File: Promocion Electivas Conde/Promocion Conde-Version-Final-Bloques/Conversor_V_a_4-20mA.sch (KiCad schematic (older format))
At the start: 11 parts

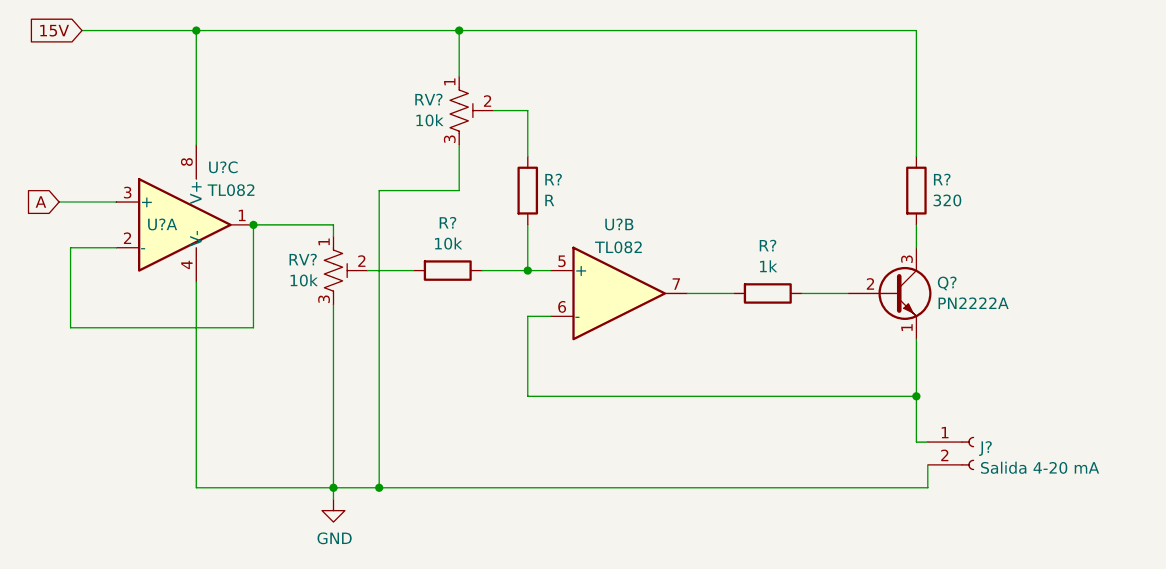
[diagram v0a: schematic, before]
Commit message: Bloques y footprint asignados
Falta elegir y asignar el de los potenciometros Rv3 y Rv7.
Las salidas K3 y K20 también...
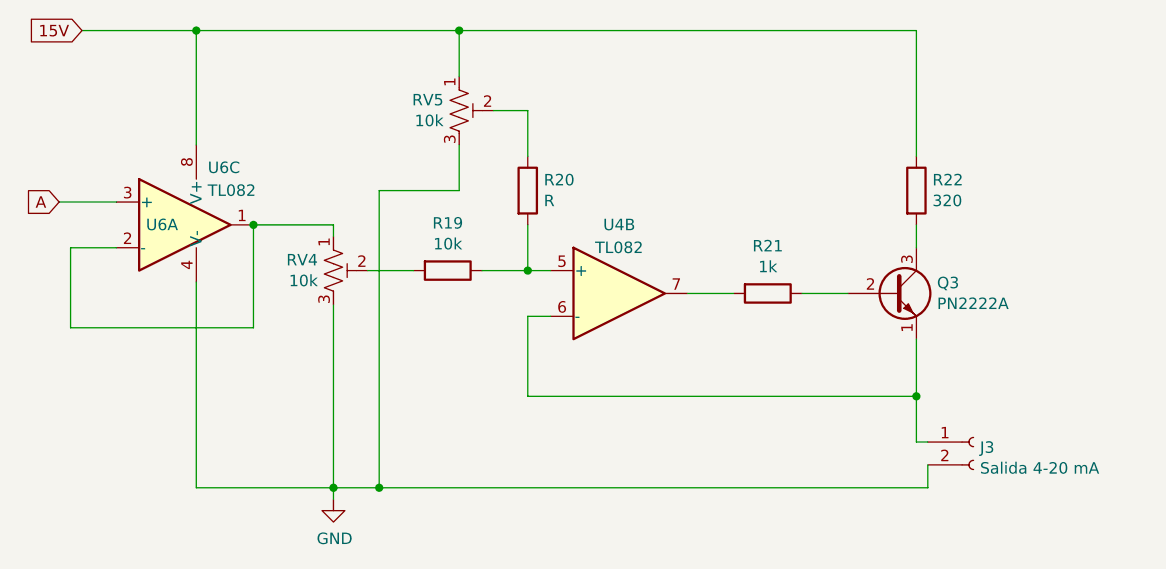
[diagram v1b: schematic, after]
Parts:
- R19, R20, R21, R22: renamed from R?; footprint (none) -> Resistor_SMD:R_0603_1608Metric_Pad0.98x0.95mm_HandSolder
- RV4, RV5: renamed from RV?; footprint (none) -> Resistor_SMD:R_0603_1608Metric_Pad0.98x0.95mm_HandSolder
- U4, U6: renamed from U?; footprint (none) -> Package_SO:SOIC-8-1EP_3.9x4.9mm_P1.27mm_EP2.29x3mm
- gave numbers to parts that had none: 2
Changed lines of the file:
@@
 $Descr A4 11693 8268
 encoding utf-8
-Sheet 5 5
+Sheet 3 6
 Title ""
 Date ""
@@
 $EndDescr
 $Comp
-L Device:R_POT_TRIM_US RV?
+L Device:R_POT_TRIM_US RV4
 U 1 1 61856B19
 P 3250 3750
-F 0 "RV?" H 3182 3796 50  0000 R CNN
+F 0 "RV4" H 3182 3796 50  0000 R CNN
 F 1 "10k" H 3182 3705 50  0000 R CNN
-F 2 "" H 3250 3750 50  0001 C CNN
+F 2 "Resistor_SMD:R_0603_1608Metric_Pad0.98x0.95mm_HandSolder" H 3250 3750 50  0001 C CNN
 F 3 "~" H 3250 3750 50  0001 C CNN
 	1    3250 3750
@@
 $EndComp
 $Comp
-L Device:R_POT_TRIM_US RV?
+L Device:R_POT_TRIM_US RV5
 U 1 1 6185887C
 P 3800 3050
-F 0 "RV?" H 3732 3096 50  0000 R CNN
+F 0 "RV5" H 3732 3096 50  0000 R CNN
 F 1 "10k" H 3732 3005 50  0000 R CNN
-F 2 "" H 3800 3050 50  0001 C CNN
+F 2 "Resistor_SMD:R_0603_1608Metric_Pad0.98x0.95mm_HandSolder" H 3800 3050 50  0001 C CNN
 F 3 "~" H 3800 3050 50  0001 C CNN
 	1    3800 3050
@@
 $EndComp
 $Comp
-L Device:R R?
+L Device:R R21
 U 1 1 61859CCC
 P 5150 3850
-F 0 "R?" V 4943 3850 50  0000 C CNN
+F 0 "R21" V 4943 3850 50  0000 C CNN
 F 1 "1k" V 5034 3850 50  0000 C CNN
-F 2 "" V 5080 3850 50  0001 C CNN
+F 2 "Resistor_SMD:R_0603_1608Metric_Pad0.98x0.95mm_HandSolder" V 5080 3850 50  0001 C CNN
 F 3 "~" H 5150 3850 50  0001 C CNN
 	1    5150 3850
@@
 $EndComp
 $Comp
-L Device:R R?
+L Device:R R22
 U 1 1 61859D46
 P 5800 3400
-F 0 "R?" H 5870 3446 50  0000 L CNN
+F 0 "R22" H 5870 3446 50  0000 L CNN
 F 1 "320" H 5870 3355 50  0000 L CNN
-F 2 "" V 5730 3400 50  0001 C CNN
+F 2 "Resistor_SMD:R_0603_1608Metric_Pad0.98x0.95mm_HandSolder" V 5730 3400 50  0001 C CNN
 F 3 "~" H 5800 3400 50  0001 C CNN
 	1    5800 3400
@@
 $EndComp
 $Comp
-L Device:R R?
+L Device:R R20
 U 1 1 6185A023
 P 4100 3400
-F 0 "R?" H 4170 3446 50  0000 L CNN
+F 0 "R20" H 4170 3446 50  0000 L CNN
 F 1 "R" H 4170 3355 50  0000 L CNN
-F 2 "" V 4030 3400 50  0001 C CNN
+F 2 "Resistor_SMD:R_0603_1608Metric_Pad0.98x0.95mm_HandSolder" V 4030 3400 50  0001 C CNN
 F 3 "~" H 4100 3400 50  0001 C CNN
 	1    4100 3400
@@
 $EndComp
 $Comp
-L Amplifier_Operational:TL082 U?
+L Amplifier_Operational:TL082 U6
 U 1 1 618669D7
 P 2600 3550
-F 0 "U?" H 2500 3550 50  0000 C CNN
+F 0 "U6" H 2500 3550 50  0000 C CNN
 F 1 "TL082" H 2550 3600 50  0001 C CNN
-F 2 "" H 2600 3550 50  0001 C CNN
+F 2 "Package_SO:SOIC-8-1EP_3.9x4.9mm_P1.27mm_EP2.29x3mm" H 2600 3550 50  0001 C CNN
 F 3 "http://www.ti.com/lit/ds/symlink/tl081.pdf" H 2600 3550 50  0001 C CNN
 	1    2600 3550
@@
 $EndComp
 $Comp
-L Amplifier_Operational:TL082 U?
+L Amplifier_Operational:TL082 U4
 U 2 1 618685B3
 P 4500 3850
-F 0 "U?" H 4500 4150 50  0000 C CNN
+F 0 "U4" H 4500 4150 50  0000 C CNN
 F 1 "TL082" H 4500 4050 50  0000 C CNN
-F 2 "" H 4500 3850 50  0001 C CNN
+F 2 "Package_SO:SOIC-8-1EP_3.9x4.9mm_P1.27mm_EP2.29x3mm" H 4500 3850 50  0001 C CNN
 F 3 "http://www.ti.com/lit/ds/symlink/tl081.pdf" H 4500 3850 50  0001 C CNN
 	2    4500 3850
@@
 $EndComp
 $Comp
-L Amplifier_Operational:TL082 U?
+L Amplifier_Operational:TL082 U6
 U 3 1 6186A0AE
 P 2750 3500
-F 0 "U?" H 2700 3700 50  0000 L CNN
+F 0 "U6" H 2700 3700 50  0000 L CNN
 F 1 "TL082" H 2700 3600 50  0000 L CNN
-F 2 "" H 2750 3500 50  0001 C CNN
+F 2 "Package_SO:SOIC-8-1EP_3.9x4.9mm_P1.27mm_EP2.29x3mm" H 2750 3500 50  0001 C CNN
 F 3 "http://www.ti.com/lit/ds/symlink/tl081.pdf" H 2750 3500 50  0001 C CNN
 	3    2750 3500
@@
 $EndComp
 $Comp
-L Transistor_BJT:PN2222A Q?
+L Transistor_BJT:PN2222A Q3
 U 1 1 6187FC89
 P 5700 3850
-F 0 "Q?" H 5890 3896 50  0000 L CNN
+F 0 "Q3" H 5890 3896 50  0000 L CNN
 F 1 "PN2222A" H 5890 3805 50  0000 L CNN
 F 2 "Package_TO_SOT_THT:TO-92_Inline" H 5900 3775 50  0001 L CIN
@@
 Connection ~ 2650 2700
 $Comp
-L power:GND #PWR?
+L power:GND #PWR0123
 U 1 1 6188776C
 P 3250 4750
-F 0 "#PWR?" H 3250 4500 50  0001 C CNN
+F 0 "#PWR0123" H 3250 4500 50  0001 C CNN
 F 1 "GND" H 3255 4577 50  0000 C CNN
 F 2 "" H 3250 4750 50  0001 C CNN
@@
 	3250 4700 3250 4750
 $Comp
-L Connector:Conn_01x02_Female J?
+L Connector:Conn_01x02_Female J3
 U 1 1 6188AFA4
 P 6050 4500
-F 0 "J?" H 6078 4476 50  0000 L CNN
+F 0 "J3" H 6078 4476 50  0000 L CNN
 F 1 "Salida 4-20 mA" H 6078 4385 50  0000 L CNN
 F 2 "" H 6050 4500 50  0001 C CNN
@@
 	3250 4700 3450 4700
 $Comp
-L Device:R R?
+L Device:R R19
 U 1 1 61858C7F
 P 3750 3750
-F 0 "R?" V 3543 3750 50  0000 C CNN
+F 0 "R19" V 3543 3750 50  0000 C CNN
 F 1 "10k" V 3634 3750 50  0000 C CNN
-F 2 "" V 3680 3750 50  0001 C CNN
+F 2 "Resistor_SMD:R_0603_1608Metric_Pad0.98x0.95mm_HandSolder" V 3680 3750 50  0001 C CNN
 F 3 "~" H 3750 3750 50  0001 C CNN
 	1    3750 3750

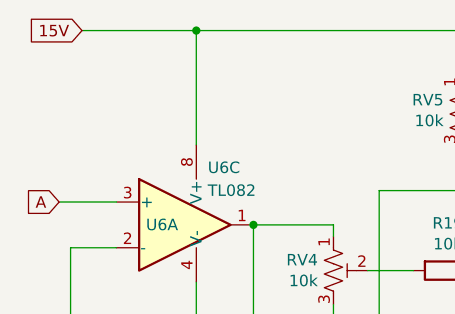
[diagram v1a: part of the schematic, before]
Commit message: Actualizacion Convertidor
Se creó el esquemático del convertidor y se hizo la conexión del mismo
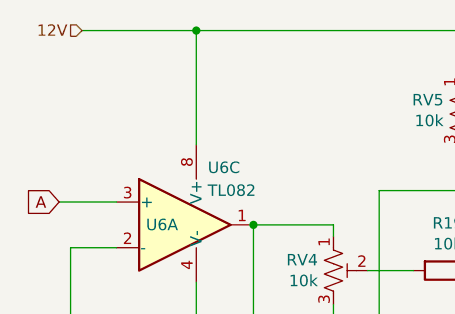
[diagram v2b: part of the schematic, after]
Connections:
- net 15V renamed 12V
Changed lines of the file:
@@
 Wire Wire Line
 	2050 3450 2300 3450
-Text GLabel 2150 2700 0    50   Input ~ 0
-15V
 Wire Wire Line
 	2150 2700 2650 2700
@@
 Wire Wire Line
 	3450 4700 5850 4700
+Text HLabel 2150 2700 0    50   Input ~ 0
+12V
 $EndSCHEMATC

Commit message: Actualizacion
Actualizo los footprints del esquematico y se inicia el PCB
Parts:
- Q3: footprint Package_TO_SOT_THT:TO-92_Inline -> Package_TO_SOT_SMD:SOT-23
- RV4, RV5: footprint Resistor_SMD:R_0603_1608Metric_Pad0.98x0.95mm_HandSolder -> Potentiometer_SMD:Potentiometer_Vishay_TS53YL_Vertical
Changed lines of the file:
@@
 F 0 "RV4" H 3182 3796 50  0000 R CNN
 F 1 "10k" H 3182 3705 50  0000 R CNN
-F 2 "Resistor_SMD:R_0603_1608Metric_Pad0.98x0.95mm_HandSolder" H 3250 3750 50  0001 C CNN
-F 3 "~" H 3250 3750 50  0001 C CNN
+F 2 "Potentiometer_SMD:Potentiometer_Vishay_TS53YL_Vertical" H 3250 3750 50  0001 C CNN
+F 3 "https://www.vishay.com/docs/51008/ts53.pdf" H 3250 3750 50  0001 C CNN
 	1    3250 3750
 	1    0    0    -1
@@
 F 0 "RV5" H 3732 3096 50  0000 R CNN
 F 1 "10k" H 3732 3005 50  0000 R CNN
-F 2 "Resistor_SMD:R_0603_1608Metric_Pad0.98x0.95mm_HandSolder" H 3800 3050 50  0001 C CNN
-F 3 "~" H 3800 3050 50  0001 C CNN
+F 2 "Potentiometer_SMD:Potentiometer_Vishay_TS53YL_Vertical" H 3800 3050 50  0001 C CNN
+F 3 "https://www.vishay.com/docs/51008/ts53.pdf" H 3800 3050 50  0001 C CNN
 	1    3800 3050
 	1    0    0    -1
@@
 F 0 "Q3" H 5890 3896 50  0000 L CNN
 F 1 "PN2222A" H 5890 3805 50  0000 L CNN
-F 2 "Package_TO_SOT_THT:TO-92_Inline" H 5900 3775 50  0001 L CIN
+F 2 "Package_TO_SOT_SMD:SOT-23" H 5900 3775 50  0001 L CIN
 F 3 "https://www.onsemi.com/pub/Collateral/PN2222-D.PDF" H 5700 3850 50  0001 L CNN
 	1    5700 3850
